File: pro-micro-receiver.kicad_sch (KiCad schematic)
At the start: 40 parts, among them J1 USB_A_PLUG, J2 Conn_01x04, SW1 SW_Push, U1 TLV740P, U2 ATmega32U4-M, U3 YJ-14015, Y1 16MHz

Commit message: Fixing the stackup Adding initial board outline Moving all elements onto the board
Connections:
- net D-OUT: now reaches J1.2 (D-), R7.1
- net D+OUT: now reaches J1.3 (D+), R5.1
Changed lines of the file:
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@@
+    (effects (font (size 1.27 1.27)) (justify left bottom))
+  )
+  (label "D+OUT" (at 50.165 97.79 0)
     (effects (font (size 1.27 1.27)) (justify left bottom))
   )
@@
     (effects (font (size 1.27 1.27)) (justify left bottom))
   )
+  (label "D-OUT" (at 50.165 93.98 0)
+    (effects (font (size 1.27 1.27)) (justify left bottom))
+  )

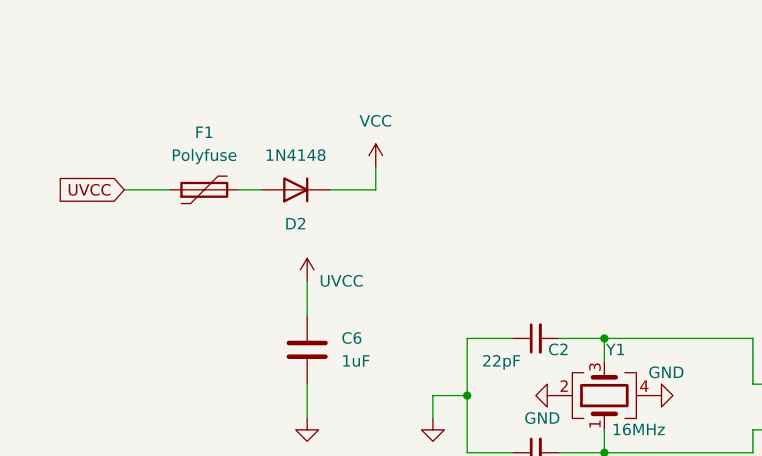
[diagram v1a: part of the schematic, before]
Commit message: Completed routing board
Removed all designators from silkscreen
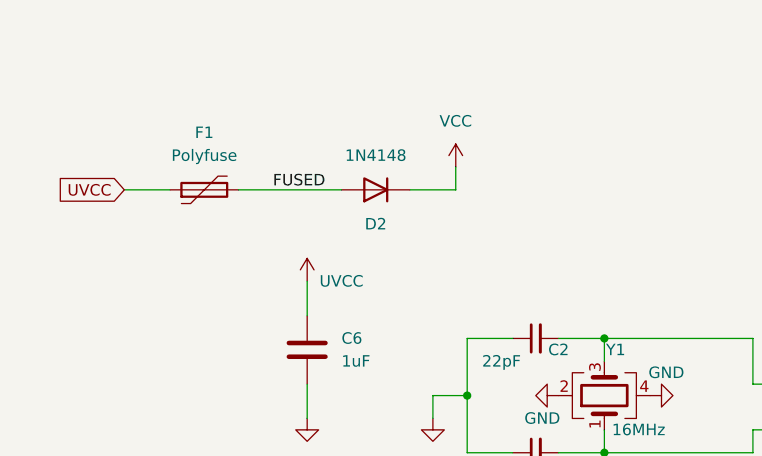
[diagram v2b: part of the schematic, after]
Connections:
- net FUSED: now reaches D2.2 (A), F1.2
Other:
- moved on the sheet: D2
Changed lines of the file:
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@@
     (stroke (width 0) (type default) (color 0 0 0 0))
   )
-  (wire (pts (xy 60.96 38.1) (xy 66.04 38.1))
+  (wire (pts (xy 69.85 38.1) (xy 74.93 38.1))
     (stroke (width 0) (type default) (color 0 0 0 0))
   )
@@
     (stroke (width 0) (type default) (color 0 0 0 0))
   )
-  (wire (pts (xy 66.04 38.1) (xy 66.04 35.56))
+  (wire (pts (xy 74.93 38.1) (xy 74.93 35.56))
     (stroke (width 0) (type default) (color 0 0 0 0))
   )
@@
     (stroke (width 0) (type default) (color 0 0 0 0))
   )
-  (wire (pts (xy 50.8 38.1) (xy 53.34 38.1))
+  (wire (pts (xy 50.8 38.1) (xy 62.23 38.1))
     (stroke (width 0) (type default) (color 0 0 0 0))
   )
@@
   )
   (label "C_A2" (at 158.75 123.19 0)
+    (effects (font (size 1.27 1.27)) (justify left bottom))
+  )
+  (label "FUSED" (at 54.61 38.1 0)
     (effects (font (size 1.27 1.27)) (justify left bottom))
   )
@@
     (pin "1")
   )
-  (symbol (lib_id "power:VCC") (at 66.04 35.56 0) (unit 1)
+  (symbol (lib_id "power:VCC") (at 74.93 35.56 0) (unit 1)
     (in_bom yes) (on_board yes) (fields_autoplaced)
-    (property "Reference" "#PWR0117" (id 0) (at 66.04 39.37 0)
-      (effects (font (size 1.27 1.27)) hide)
-    )
-    (property "Value" "VCC" (id 1) (at 66.04 30.48 0))
-    (property "Footprint" "" (id 2) (at 66.04 35.56 0)
-      (effects (font (size 1.27 1.27)) hide)
-    )
-    (property "Datasheet" "" (id 3) (at 66.04 35.56 0)
+    (property "Reference" "#PWR0117" (id 0) (at 74.93 39.37 0)
+      (effects (font (size 1.27 1.27)) hide)
+    )
+    (property "Value" "VCC" (id 1) (at 74.93 30.48 0))
+    (property "Footprint" "" (id 2) (at 74.93 35.56 0)
+      (effects (font (size 1.27 1.27)) hide)
+    )
+    (property "Datasheet" "" (id 3) (at 74.93 35.56 0)
       (effects (font (size 1.27 1.27)) hide)
     )
@@
     (pin "1")
   )
-  (symbol (lib_id "Diode:1N4148") (at 57.15 38.1 180) (unit 1)
+  (symbol (lib_id "Diode:1N4148") (at 66.04 38.1 180) (unit 1)
     (in_bom yes) (on_board yes)
-    (property "Reference" "D2" (id 0) (at 57.15 41.91 0))
-    (property "Value" "1N4148" (id 1) (at 57.15 34.29 0))
-    (property "Footprint" "Diode_SMD_AKL:D_SOD-123" (id 2) (at 57.15 38.1 0)
-      (effects (font (size 1.27 1.27)) hide)
-    )
-    (property "Datasheet" "https://assets.nexperia.com/documents/data-sheet/1N4148_1N4448.pdf" (id 3) (at 57.15 38.1 0)
-      (effects (font (size 1.27 1.27)) hide)
-    )
+    (property "Reference" "D2" (id 0) (at 66.04 41.91 0))
+    (property "Value" "1N4148" (id 1) (at 66.04 34.29 0))
+    (property "Footprint" "Diode_SMD_AKL:D_SOD-123" (id 2) (at 66.04 38.1 0)
+      (effects (font (size 1.27 1.27)) hide)
+    )
+    (property "Datasheet" "https://assets.nexperia.com/documents/data-sheet/1N4148_1N4448.pdf" (id 3) (at 66.04 38.1 0)
+      (effects (font (size 1.27 1.27)) hide)
+    )

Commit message: Adding testpoints in schematic
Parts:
- added TP? (x13): TestPoint, TestPoint:TestPoint_Pad_D2.0mm, symbol Connector:TestPoint
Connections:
- net +3V3: now also TP?.1
- net GND: now also TP?.1
- net RXI: now also TP?.1
- net SWCLK: now also TP?.1
- net SWDIO: now also TP?.1
- net TXO: now also TP?.1
- net TXODIV: now also TP?.1
- net UVCC: now also TP?.1
- net VCC: now also TP?.1
- net PD7: now reaches U2.27 (PD7)
- net PD7: now also TP?.1
- net PB4: now reaches U2.28 (PB4)
- net PB4: now also TP?.1
- net PB5: now reaches U2.29 (PB5)
- net PB5: now also TP?.1
- net PB6: now reaches U2.30 (PB6)
- net PB6: now also TP?.1
- no-connect marks 46 -> 42

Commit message: Adding testpoints to PCB
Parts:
- removed TP? (x2): TestPoint, TestPoint:TestPoint_Pad_D2.0mm, symbol Connector:TestPoint
- TP1, TP11, TP12, TP13, TP2, TP3, TP4, TP5, TP6, TP7, TP8: renamed from TP?; footprint TestPoint:TestPoint_Pad_D2.0mm -> TestPoint:TestPoint_Pad_D1.5mm
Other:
- moved on the sheet: TP11, TP12, TP13

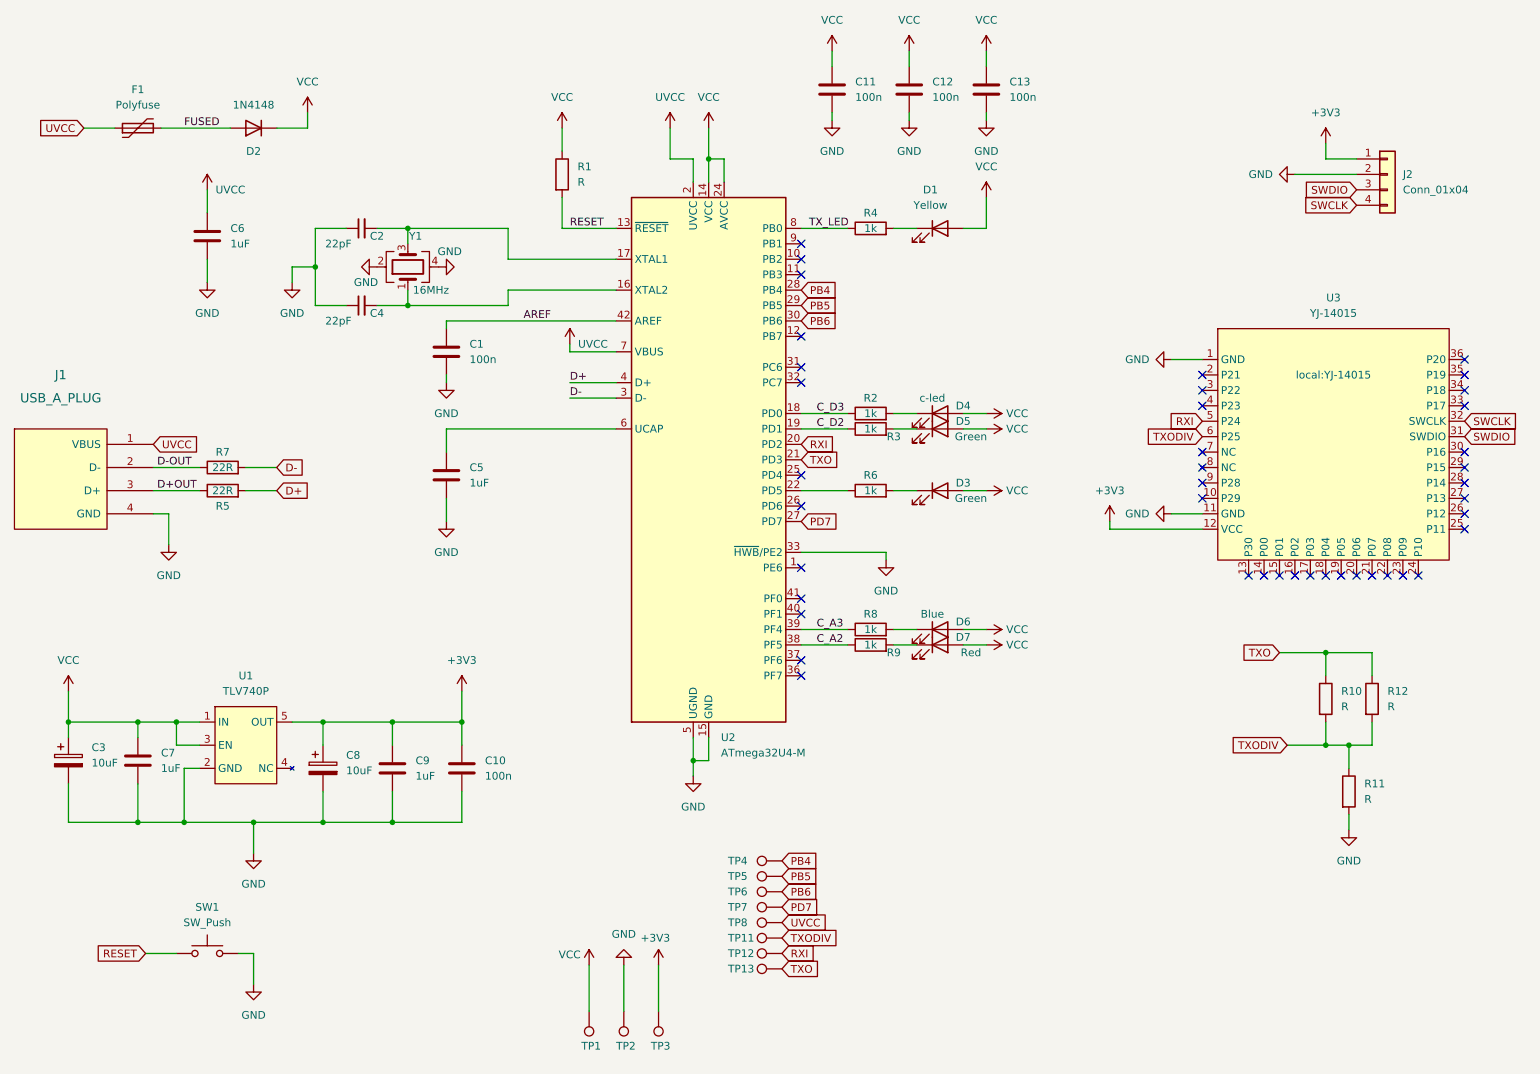
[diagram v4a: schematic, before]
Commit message: Adding missing values for resistors
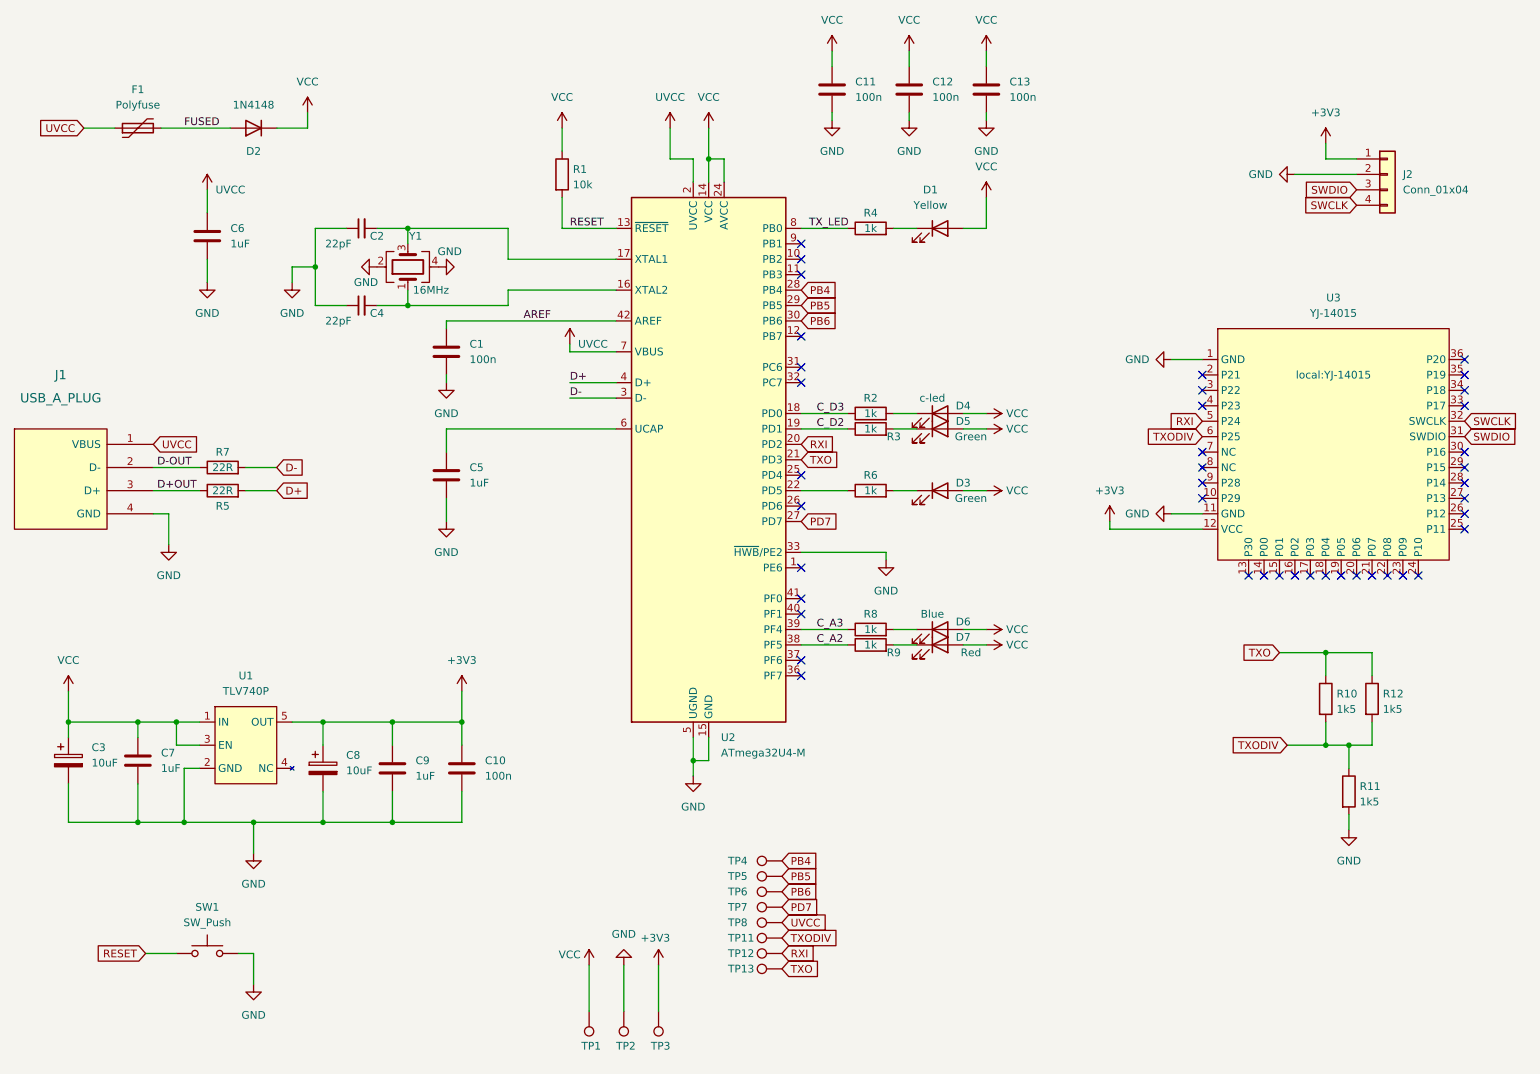
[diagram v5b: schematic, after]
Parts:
- R1: value R -> 10k
- R10, R11, R12: value R -> 1k5
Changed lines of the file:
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@@
   (symbol (lib_id "Device:R") (at 246.38 147.32 0) (unit 1)
     (in_bom yes) (on_board yes) (fields_autoplaced)
-    (property "Reference" "R11" (id 0) (at 248.92 146.0499 0)
-      (effects (font (size 1.27 1.27)) (justify left))
-    )
-    (property "Value" "R" (id 1) (at 248.92 148.5899 0)
+    (property "Reference" "R11" (id 0) (at 248.158 146.4853 0)
+      (effects (font (size 1.27 1.27)) (justify left))
+    )
+    (property "Value" "1k5" (id 1) (at 248.158 149.0222 0)
       (effects (font (size 1.27 1.27)) (justify left))
     )
@@
   (symbol (lib_id "Device:R") (at 116.84 45.72 0) (unit 1)
     (in_bom yes) (on_board yes) (fields_autoplaced)
-    (property "Reference" "R1" (id 0) (at 119.38 44.4499 0)
-      (effects (font (size 1.27 1.27)) (justify left))
-    )
-    (property "Value" "R" (id 1) (at 119.38 46.9899 0)
+    (property "Reference" "R1" (id 0) (at 118.618 44.8853 0)
+      (effects (font (size 1.27 1.27)) (justify left))
+    )
+    (property "Value" "10k" (id 1) (at 118.618 47.4222 0)
       (effects (font (size 1.27 1.27)) (justify left))
     )
@@
   (symbol (lib_id "Device:R") (at 242.57 132.08 0) (unit 1)
     (in_bom yes) (on_board yes) (fields_autoplaced)
-    (property "Reference" "R10" (id 0) (at 245.11 130.8099 0)
-      (effects (font (size 1.27 1.27)) (justify left))
-    )
-    (property "Value" "R" (id 1) (at 245.11 133.3499 0)
+    (property "Reference" "R10" (id 0) (at 244.348 131.2453 0)
+      (effects (font (size 1.27 1.27)) (justify left))
+    )
+    (property "Value" "1k5" (id 1) (at 244.348 133.7822 0)
       (effects (font (size 1.27 1.27)) (justify left))
     )
@@
   (symbol (lib_id "Device:R") (at 250.19 132.08 0) (unit 1)
     (in_bom yes) (on_board yes) (fields_autoplaced)
-    (property "Reference" "R12" (id 0) (at 252.73 130.8099 0)
-      (effects (font (size 1.27 1.27)) (justify left))
-    )
-    (property "Value" "R" (id 1) (at 252.73 133.3499 0)
+    (property "Reference" "R12" (id 0) (at 251.968 131.2453 0)
+      (effects (font (size 1.27 1.27)) (justify left))
+    )
+    (property "Value" "1k5" (id 1) (at 251.968 133.7822 0)
       (effects (font (size 1.27 1.27)) (justify left))
     )
@@
     )
     (path "/68cfcabf-5c53-4d28-8382-472cb1a61a06"
-      (reference "R1") (unit 1) (value "R") (footprint "Resistor_SMD_AKL:R_0603_1608Metric")
+      (reference "R1") (unit 1) (value "10k") (footprint "Resistor_SMD_AKL:R_0603_1608Metric")
     )
     (path "/c006ed7f-5a48-401e-b166-f7a201bd6b02"
@@
     )
     (path "/ebb7e7d5-1bbd-4557-8a40-1dabbceacefd"
-      (reference "R10") (unit 1) (value "R") (footprint "Resistor_SMD_AKL:R_0603_1608Metric")
+      (reference "R10") (unit 1) (value "1k5") (footprint "Resistor_SMD_AKL:R_0603_1608Metric")
     )
     (path "/2cef3b47-da5e-4b1f-9aed-ba31e0a5b888"
-      (reference "R11") (unit 1) (value "R") (footprint "Resistor_SMD_AKL:R_0603_1608Metric")
+      (reference "R11") (unit 1) (value "1k5") (footprint "Resistor_SMD_AKL:R_0603_1608Metric")
     )
     (path "/ec2302d1-5854-4490-9af2-0903c10c4e8c"
-      (reference "R12") (unit 1) (value "R") (footprint "Resistor_SMD_AKL:R_0603_1608Metric")
+      (reference "R12") (unit 1) (value "1k5") (footprint "Resistor_SMD_AKL:R_0603_1608Metric")
     )
     (path "/6e75b780-a244-4719-91d0-be13f3a30465"

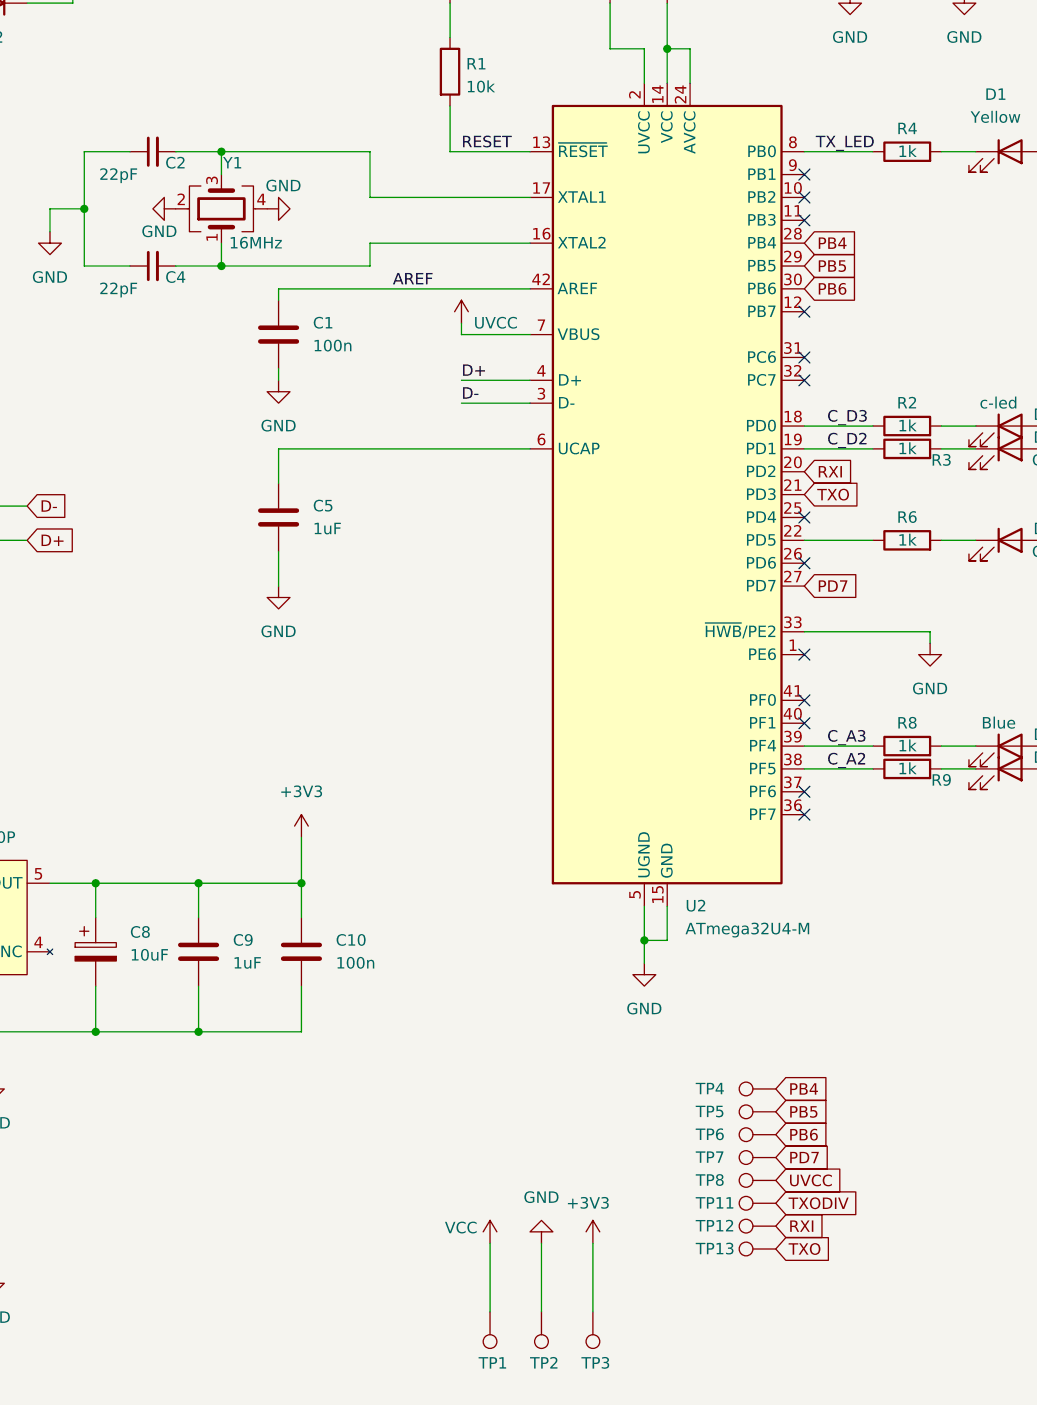
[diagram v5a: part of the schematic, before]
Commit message: Adding BOM for assembly and programming port on the back
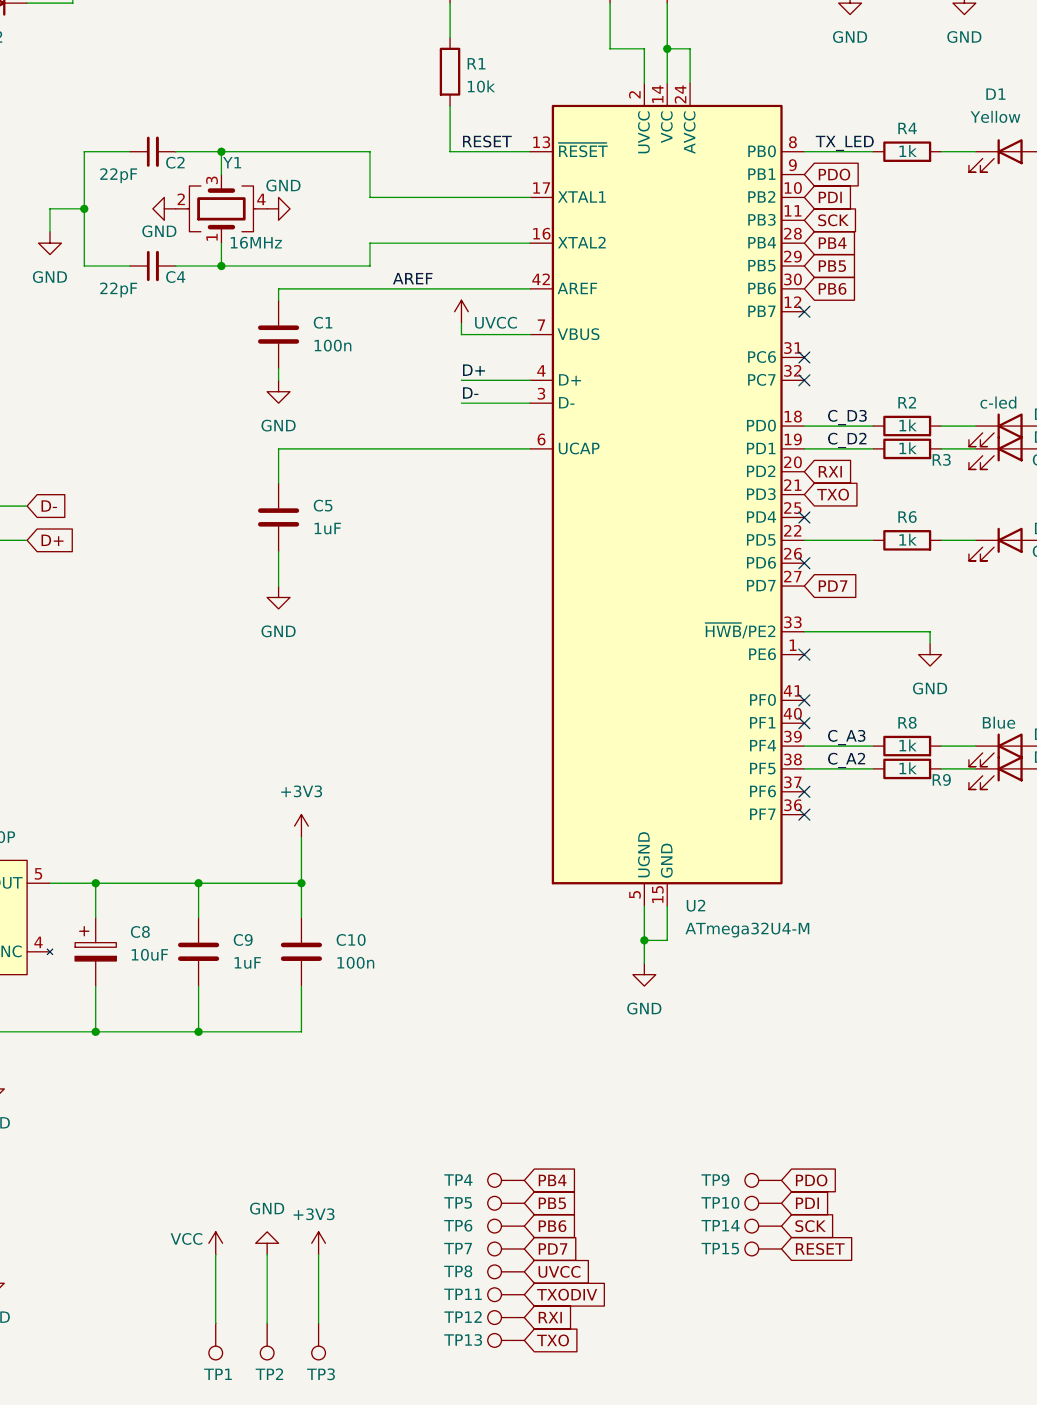
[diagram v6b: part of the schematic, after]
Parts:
- added TP10, TP14, TP15, TP9: TestPoint, TestPoint:TestPoint_Pad_D1.5mm, symbol Connector:TestPoint
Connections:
- net RESET: now also TP15.1
- net PDI: now reaches U2.10 (PB2)
- net PDI: now also TP10.1
- net SCK: now reaches U2.11 (PB3)
- net SCK: now also TP14.1
- net PDO: now reaches U2.9 (PB1)
- net PDO: now also TP9.1
- no-connect marks 42 -> 39
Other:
- moved on the sheet: TP1, TP11, TP12, TP13, TP2, TP3, TP4, TP5, TP6, TP7, TP8
